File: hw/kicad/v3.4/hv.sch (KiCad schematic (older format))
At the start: 7 parts

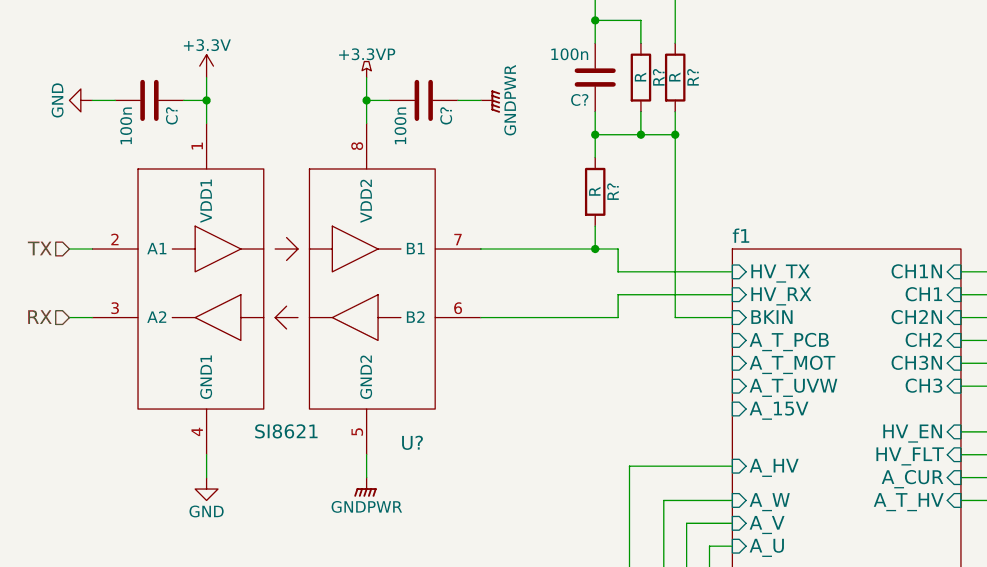
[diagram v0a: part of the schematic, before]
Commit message: gitignore kicad bak files, hv tx fix
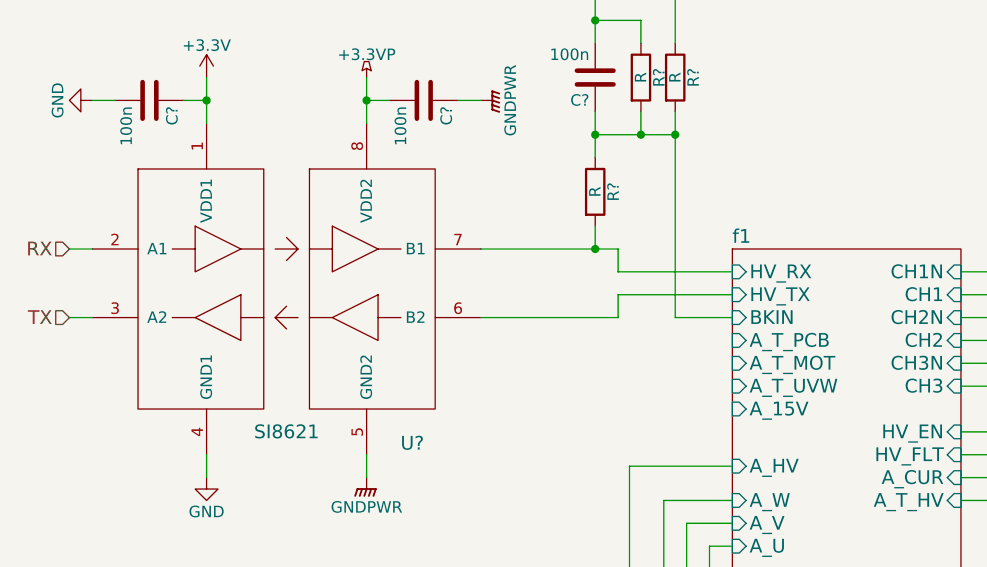
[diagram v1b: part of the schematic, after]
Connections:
- net RX: now also U?.2 (A1); no longer U?.3 (A2)
- net TX: now also U?.3 (A2); no longer U?.2 (A1)
- net f1/HV_RX: now also R?.2, U?.7 (B1); no longer U?.6 (B2)
- net f1/HV_TX: now also U?.6 (B2); no longer R?.2, U?.7 (B1)
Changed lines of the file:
@@
 EESchema Schematic File Version 2
+LIBS:power
 LIBS:stmbl_3.4-cache
 EELAYER 25 0
@@
 F6 "CH2" I R 7000 2200 60
 F7 "CH3" I R 7000 2400 60
-F8 "HV_TX" I L 6000 1900 60
-F9 "HV_RX" I L 6000 2000 60
+F8 "HV_TX" I L 6000 2000 60
+F9 "HV_RX" I L 6000 1900 60
 F10 "A_15V" I L 6000 2500 60
 F11 "A_HV" I L 6000 2750 60
@@
 Wire Wire Line
 	5550 2750 6000 2750
+Text HLabel 3100 2100 0    60   Input ~ 0
+TX
 Text HLabel 3100 1800 0    60   Input ~ 0
-TX
-Text HLabel 3100 2100 0    60   Input ~ 0
 RX
 $Comp

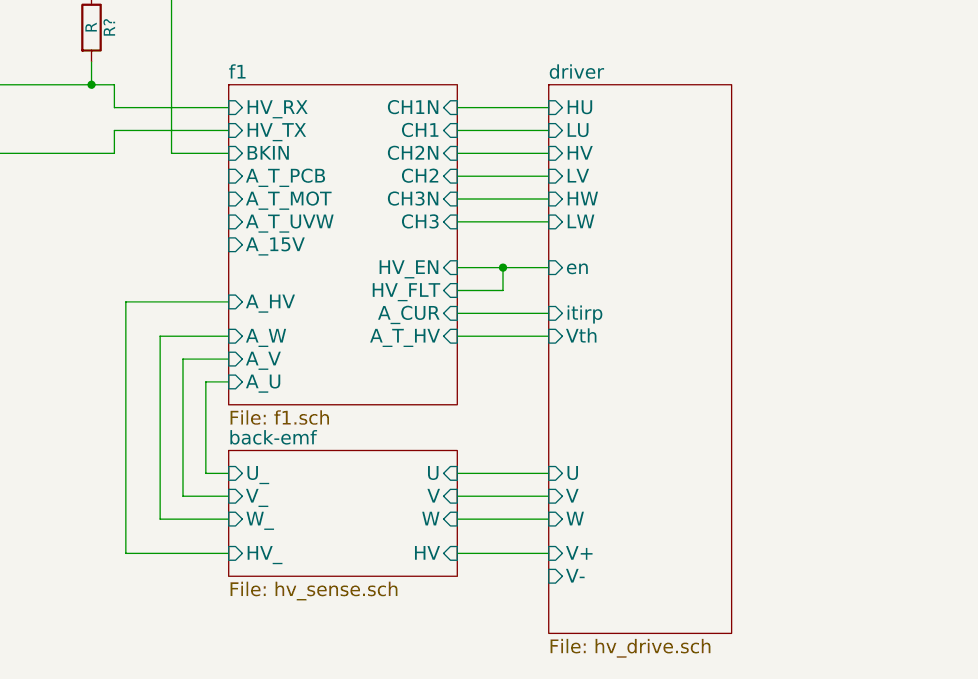
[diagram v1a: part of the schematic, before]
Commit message: +iram256
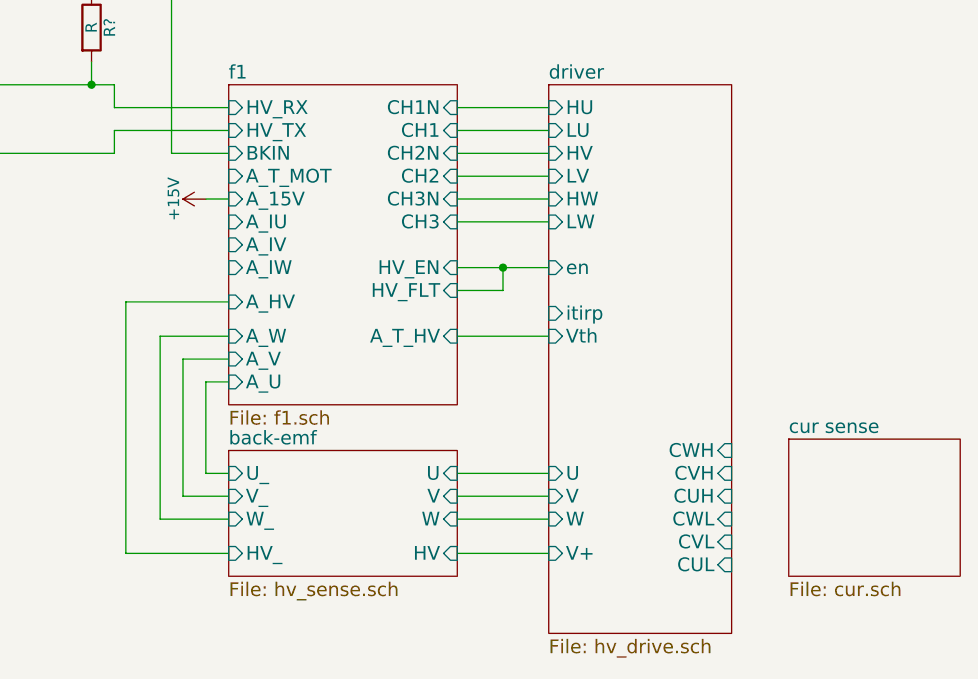
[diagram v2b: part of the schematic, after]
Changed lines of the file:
@@
 $Descr A4 11693 8268
 encoding utf-8
-Sheet 2 14
+Sheet 2 15
 Title ""
 Date ""
@@
 F8 "HV_TX" I L 6000 2000 60
 F9 "HV_RX" I L 6000 1900 60
-F10 "A_15V" I L 6000 2500 60
+F10 "A_15V" I L 6000 2300 60
 F11 "A_HV" I L 6000 2750 60
 F12 "A_U" I L 6000 3100 60
 F13 "A_V" I L 6000 3000 60
 F14 "A_W" I L 6000 2900 60
-F15 "A_CUR" I R 7000 2800 60
-F16 "A_T_HV" I R 7000 2900 60
-F17 "A_T_UVW" I L 6000 2400 60
-F18 "A_T_MOT" I L 6000 2300 60
-F19 "A_T_PCB" I L 6000 2200 60
-F20 "HV_EN" I R 7000 2600 60
-F21 "HV_FLT" I R 7000 2700 60
-F22 "BKIN" I L 6000 2100 60
+F15 "A_T_HV" I R 7000 2900 60
+F16 "A_T_MOT" I L 6000 2200 60
+F17 "HV_EN" I R 7000 2600 60
+F18 "HV_FLT" I R 7000 2700 60
+F19 "BKIN" I L 6000 2100 60
+F20 "A_IU" I L 6000 2400 60
+F21 "A_IV" I L 6000 2500 60
+F22 "A_IW" I L 6000 2600 60
 $EndSheet
 $Sheet
@@
 F3 "V" I L 7400 3600 60
 F4 "U" I L 7400 3500 60
-F5 "V-" I L 7400 3950 60
-F6 "V+" I L 7400 3850 60
-F7 "Vth" I L 7400 2900 60
-F8 "HU" I L 7400 1900 60
-F9 "LU" I L 7400 2000 60
-F10 "HV" I L 7400 2100 60
-F11 "LV" I L 7400 2200 60
-F12 "HW" I L 7400 2300 60
-F13 "LW" I L 7400 2400 60
-F14 "en" I L 7400 2600 60
-F15 "itirp" I L 7400 2800 60
+F5 "V+" I L 7400 3850 60
+F6 "Vth" I L 7400 2900 60
+F7 "HU" I L 7400 1900 60
+F8 "LU" I L 7400 2000 60
+F9 "HV" I L 7400 2100 60
+F10 "LV" I L 7400 2200 60
+F11 "HW" I L 7400 2300 60
+F12 "LW" I L 7400 2400 60
+F13 "en" I L 7400 2600 60
+F14 "itirp" I L 7400 2800 60
+F15 "CUL" I R 8200 3900 60
+F16 "CVL" I R 8200 3800 60
+F17 "CWL" I R 8200 3700 60
+F18 "CUH" I R 8200 3600 60
+F19 "CVH" I R 8200 3500 60
+F20 "CWH" I R 8200 3400 60
 $EndSheet
 Wire Wire Line
@@
 	7200 2700 7200 2600
 Connection ~ 7200 2600
-Wire Wire Line
-	7000 2800 7400 2800
 Wire Wire Line
 	7000 2900 7400 2900
@@
 	5750 2100 6000 2100
 Connection ~ 5750 1300
+$Comp
+L +15V #PWR?
+U 1 1 56695890
+P 5900 2300
+F 0 "#PWR?" H 5900 2150 50  0001 C CNN
+F 1 "+15V" H 5900 2440 50  0000 C CNN
+F 2 "" H 5900 2300 60  0000 C CNN
+F 3 "" H 5900 2300 60  0000 C CNN
+	1    5900 2300
+	0    -1   -1   0
+$EndComp
+Wire Wire Line
+	5900 2300 6000 2300
+$Sheet
+S 8450 3350 750  600
+U 566962E3
+F0 "cur sense" 60
+F1 "cur.sch" 60
+$EndSheet
 $EndSCHEMATC

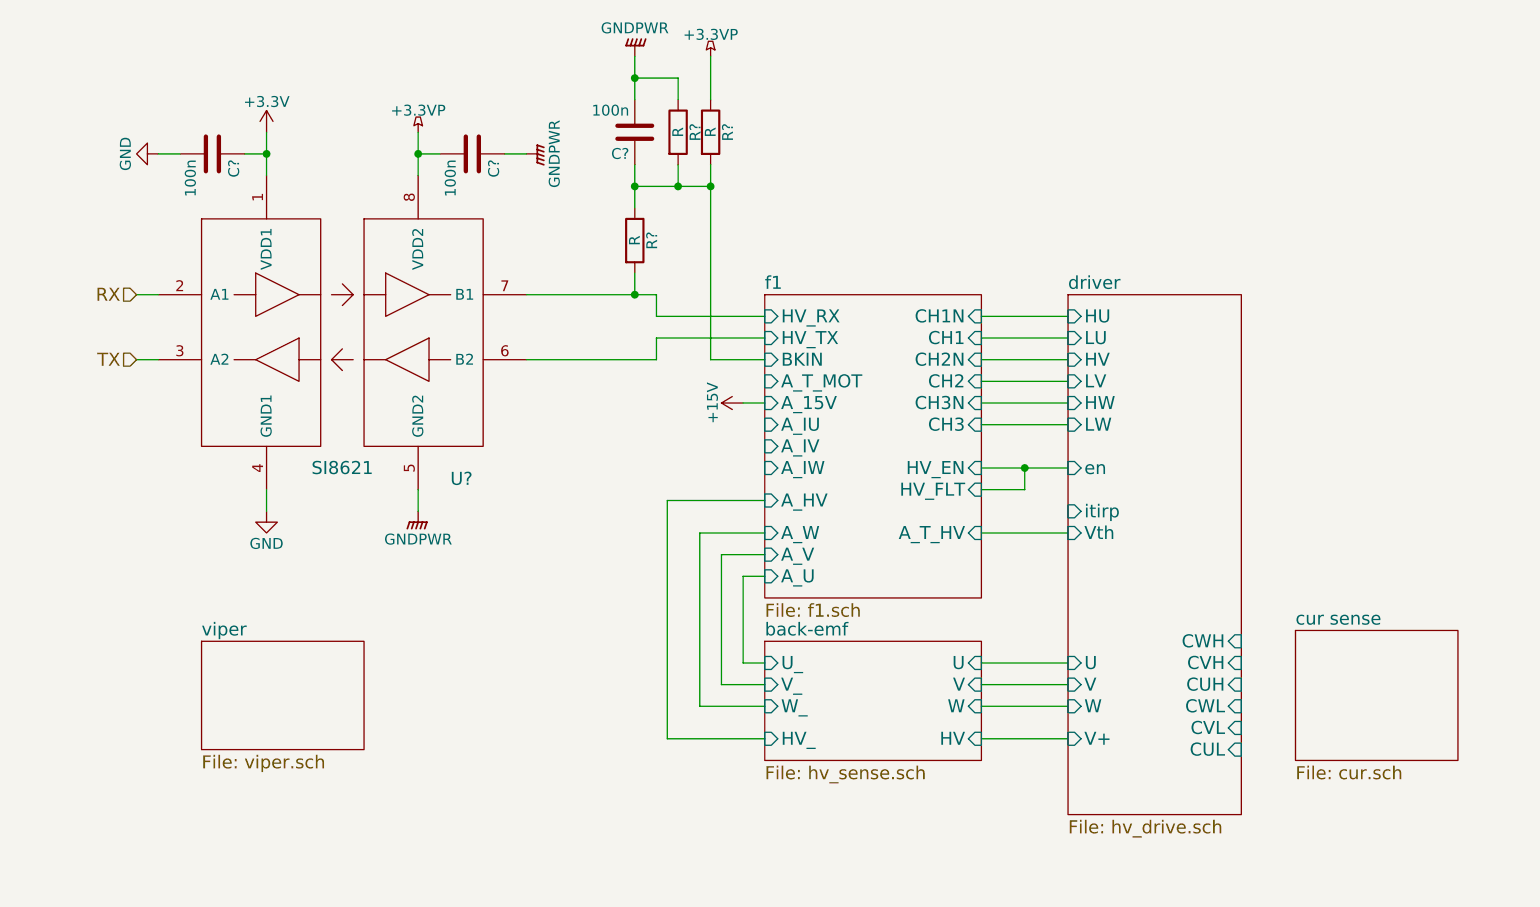
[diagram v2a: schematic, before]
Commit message: +cur sense, f4 pin remap
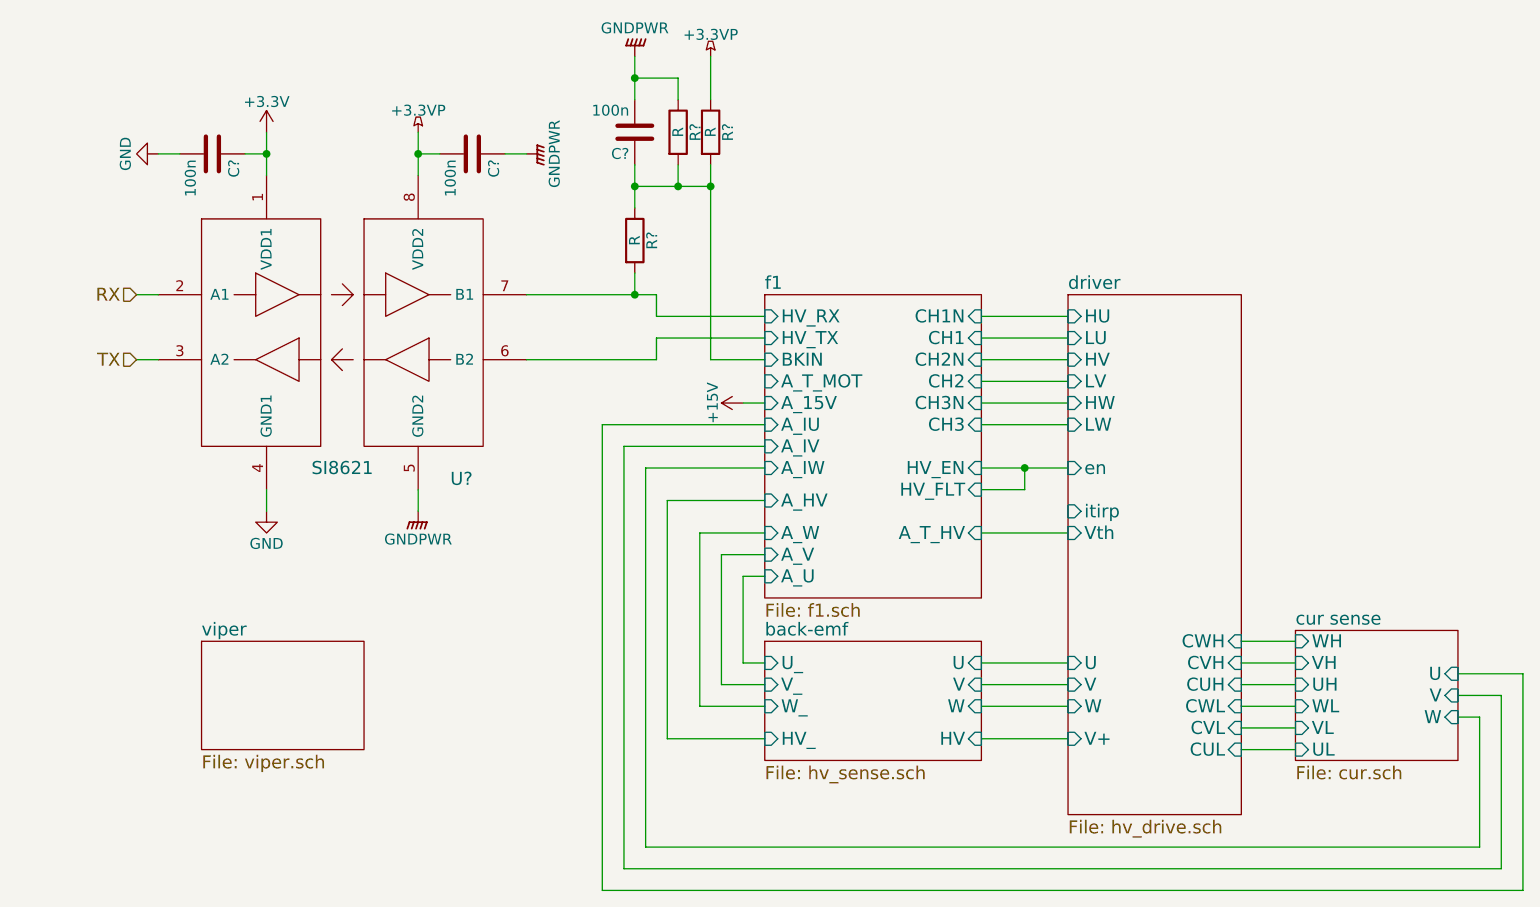
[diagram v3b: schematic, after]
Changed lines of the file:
@@
 F0 "cur sense" 60
 F1 "cur.sch" 60
+F2 "VH" I L 8450 3500 60
+F3 "VL" I L 8450 3800 60
+F4 "V" I R 9200 3650 60
+F5 "WH" I L 8450 3400 60
+F6 "WL" I L 8450 3700 60
+F7 "W" I R 9200 3750 60
+F8 "UH" I L 8450 3600 60
+F9 "UL" I L 8450 3900 60
+F10 "U" I R 9200 3550 60
 $EndSheet
+Wire Wire Line
+	8200 3900 8450 3900
+Wire Wire Line
+	8200 3800 8450 3800
+Wire Wire Line
+	8200 3700 8450 3700
+Wire Wire Line
+	8200 3600 8450 3600
+Wire Wire Line
+	8200 3500 8450 3500
+Wire Wire Line
+	8200 3400 8450 3400
+Wire Wire Line
+	9200 3750 9300 3750
+Wire Wire Line
+	9300 3750 9300 4350
+Wire Wire Line
+	9300 4350 5450 4350
+Wire Wire Line
+	5450 4350 5450 2600
+Wire Wire Line
+	5450 2600 6000 2600
+Wire Wire Line
+	6000 2500 5350 2500
+Wire Wire Line
+	5350 2500 5350 4450
+Wire Wire Line
+	5350 4450 9400 4450
+Wire Wire Line
+	9400 4450 9400 3650
+Wire Wire Line
+	9400 3650 9200 3650
+Wire Wire Line
+	9200 3550 9500 3550
+Wire Wire Line
+	9500 3550 9500 4550
+Wire Wire Line
+	9500 4550 5250 4550
+Wire Wire Line
+	5250 4550 5250 2400
+Wire Wire Line
+	5250 2400 6000 2400
 $EndSCHEMATC

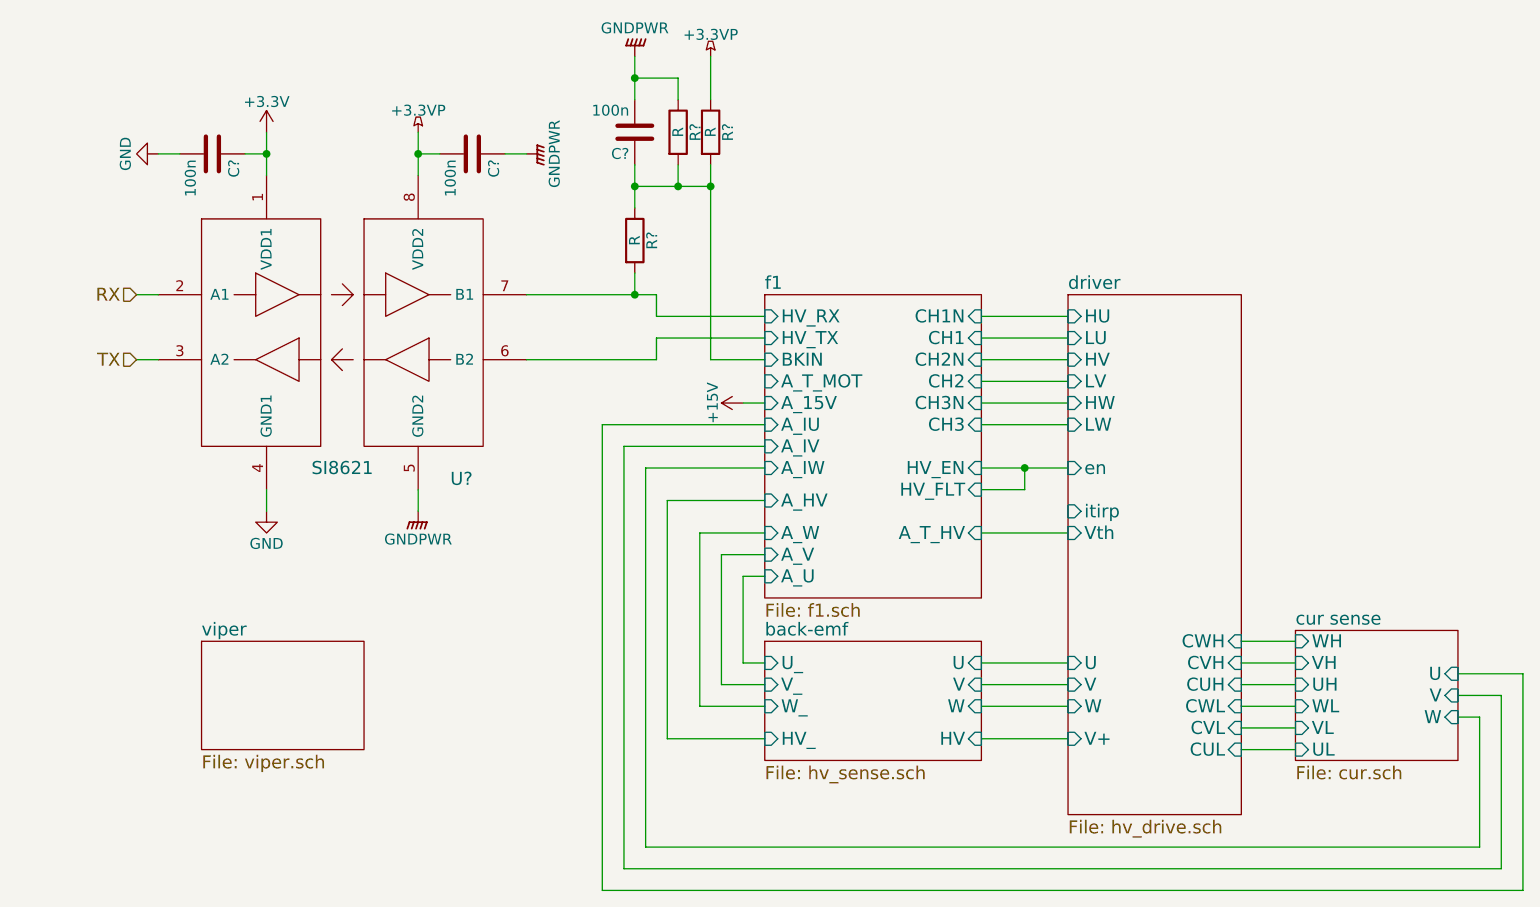
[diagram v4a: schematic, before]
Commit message: +f1 3.3V, viper fix
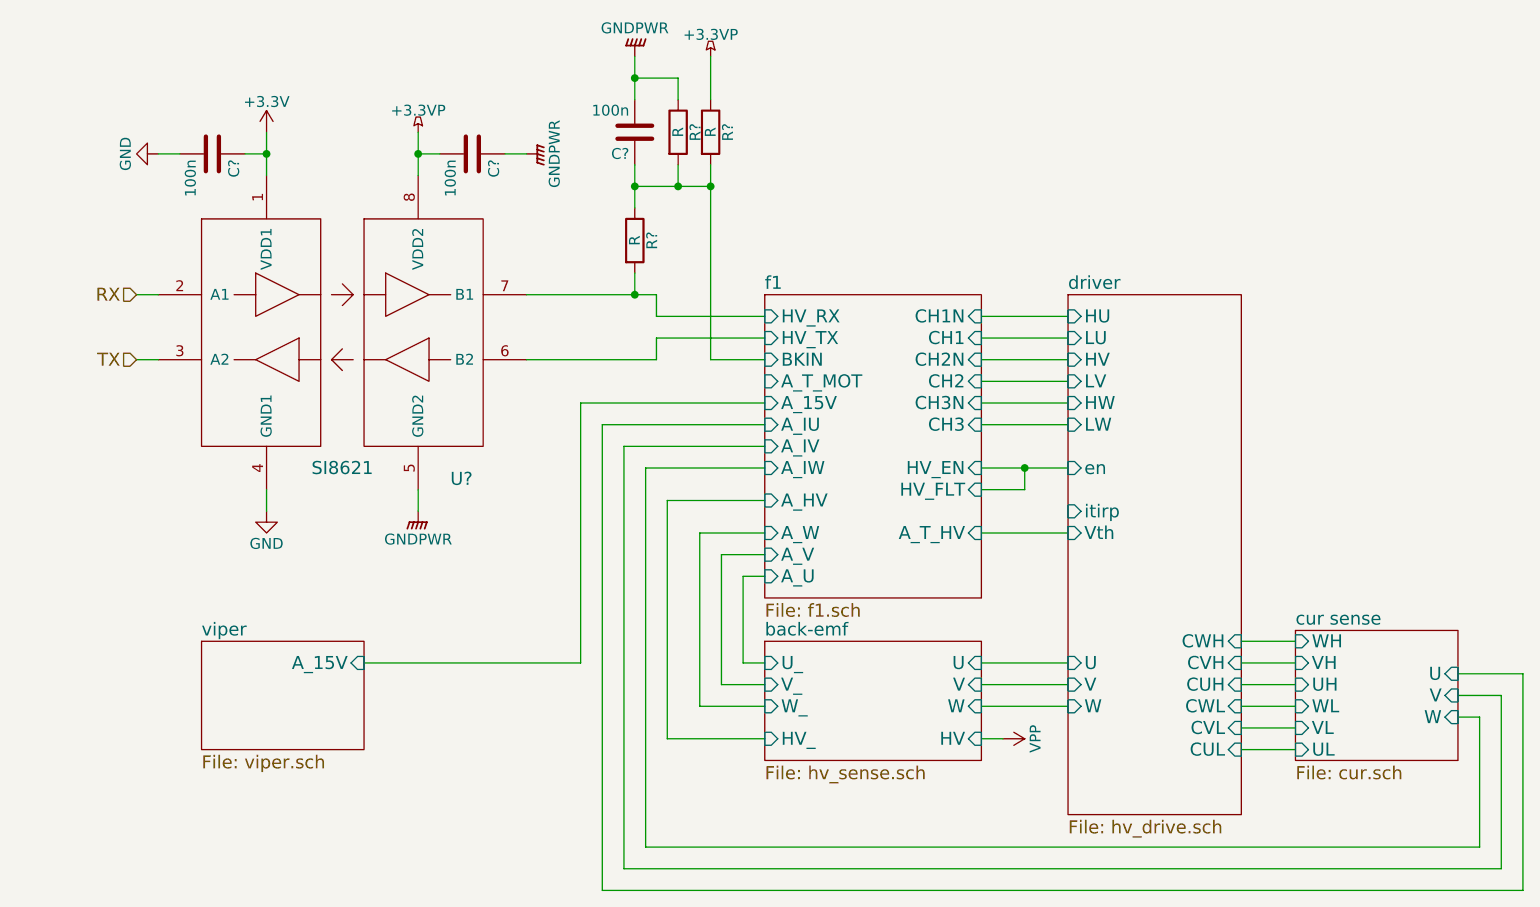
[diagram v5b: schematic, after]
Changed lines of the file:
@@
 F0 "viper" 60
 F1 "viper.sch" 60
+F2 "A_15V" I R 4150 3500 60
 $EndSheet
 $Sheet
@@
 F3 "V" I L 7400 3600 60
 F4 "U" I L 7400 3500 60
-F5 "V+" I L 7400 3850 60
-F6 "Vth" I L 7400 2900 60
-F7 "HU" I L 7400 1900 60
-F8 "LU" I L 7400 2000 60
-F9 "HV" I L 7400 2100 60
-F10 "LV" I L 7400 2200 60
-F11 "HW" I L 7400 2300 60
-F12 "LW" I L 7400 2400 60
-F13 "en" I L 7400 2600 60
-F14 "itirp" I L 7400 2800 60
-F15 "CUL" I R 8200 3900 60
-F16 "CVL" I R 8200 3800 60
-F17 "CWL" I R 8200 3700 60
-F18 "CUH" I R 8200 3600 60
-F19 "CVH" I R 8200 3500 60
-F20 "CWH" I R 8200 3400 60
+F5 "Vth" I L 7400 2900 60
+F6 "HU" I L 7400 1900 60
+F7 "LU" I L 7400 2000 60
+F8 "HV" I L 7400 2100 60
+F9 "LV" I L 7400 2200 60
+F10 "HW" I L 7400 2300 60
+F11 "LW" I L 7400 2400 60
+F12 "en" I L 7400 2600 60
+F13 "itirp" I L 7400 2800 60
+F14 "CUL" I R 8200 3900 60
+F15 "CVL" I R 8200 3800 60
+F16 "CWL" I R 8200 3700 60
+F17 "CUH" I R 8200 3600 60
+F18 "CVH" I R 8200 3500 60
+F19 "CWH" I R 8200 3400 60
 $EndSheet
 Wire Wire Line
@@
 Wire Wire Line
 	7000 3700 7400 3700
-Wire Wire Line
-	7000 3850 7400 3850
 Wire Wire Line
 	6000 3100 5900 3100
@@
 	5750 2100 6000 2100
 Connection ~ 5750 1300
-$Comp
-L +15V #PWR?
-U 1 1 56695890
-P 5900 2300
-F 0 "#PWR?" H 5900 2150 50  0001 C CNN
-F 1 "+15V" H 5900 2440 50  0000 C CNN
-F 2 "" H 5900 2300 60  0000 C CNN
-F 3 "" H 5900 2300 60  0000 C CNN
-	1    5900 2300
-	0    -1   -1   0
-$EndComp
-Wire Wire Line
-	5900 2300 6000 2300
+Wire Wire Line
+	5150 2300 6000 2300
 $Sheet
 S 8450 3350 750  600
@@
 Wire Wire Line
 	5250 2400 6000 2400
+$Comp
+L VPP #PWR?
+U 1 1 566CF982
+P 7100 3850
+F 0 "#PWR?" H 7100 3700 50  0001 C CNN
+F 1 "VPP" H 7100 4000 50  0000 C CNN
+F 2 "" H 7100 3850 60  0000 C CNN
+F 3 "" H 7100 3850 60  0000 C CNN
+	1    7100 3850
+	0    1    1    0
+$EndComp
+Wire Wire Line
+	7000 3850 7100 3850
+Wire Wire Line
+	5150 2300 5150 3500
+Wire Wire Line
+	5150 3500 4150 3500
 $EndSCHEMATC
